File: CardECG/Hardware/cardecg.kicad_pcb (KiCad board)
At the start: 2 copper layers, 58 parts, among them CN1 2TAP, P1 PROG, P2 BATTERY, Q1 NTR1P02T1, Q2 NTR1P02T1, Q3 NTR1P02T1, Q4 NTR1P02T1, Q5 NMOS_GSD, Q6 NMOS_GSD, Q7 NTR1P02T1, Q8 NTR1P02T1, U1 LMV341, U2 TPS717, U3 ADuC7061, U4 SSD1306, U5 creditcard, U6 DNP, U7 DNP

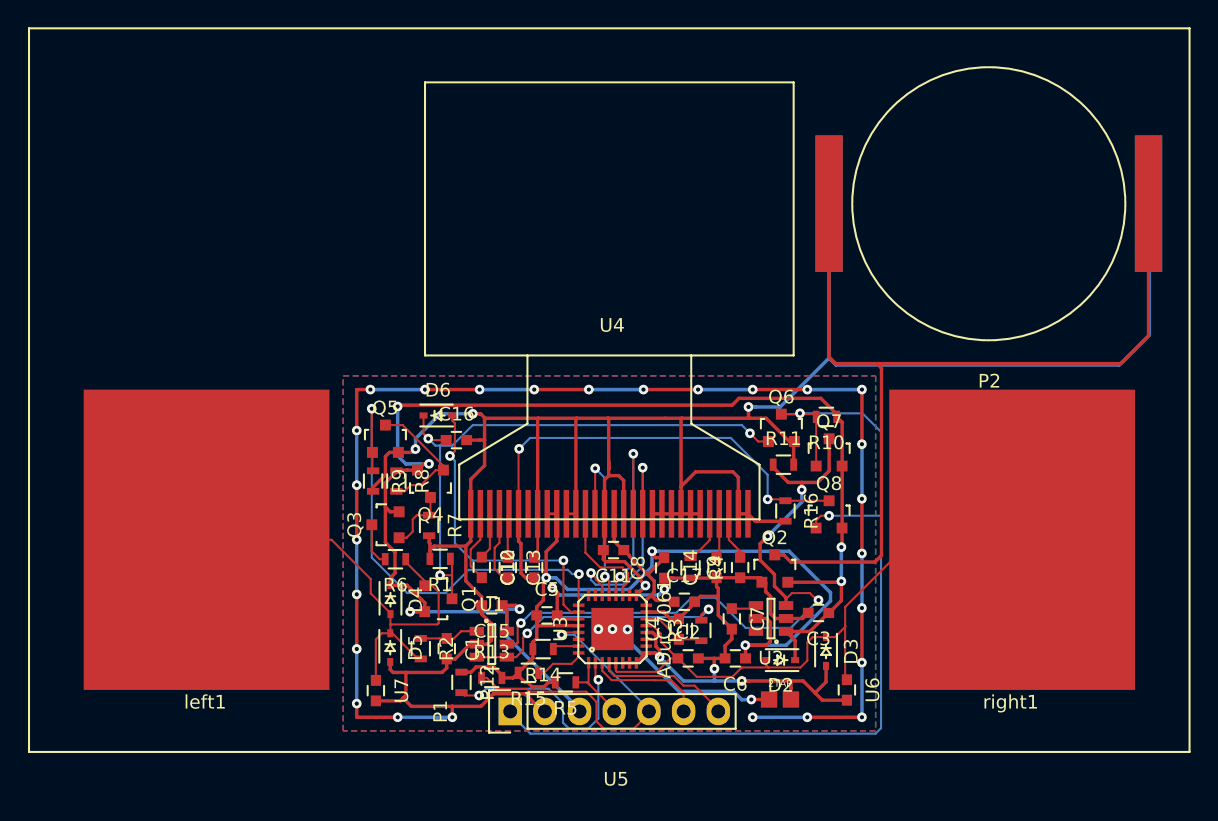
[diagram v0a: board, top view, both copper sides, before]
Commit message: Battery holder improvements.
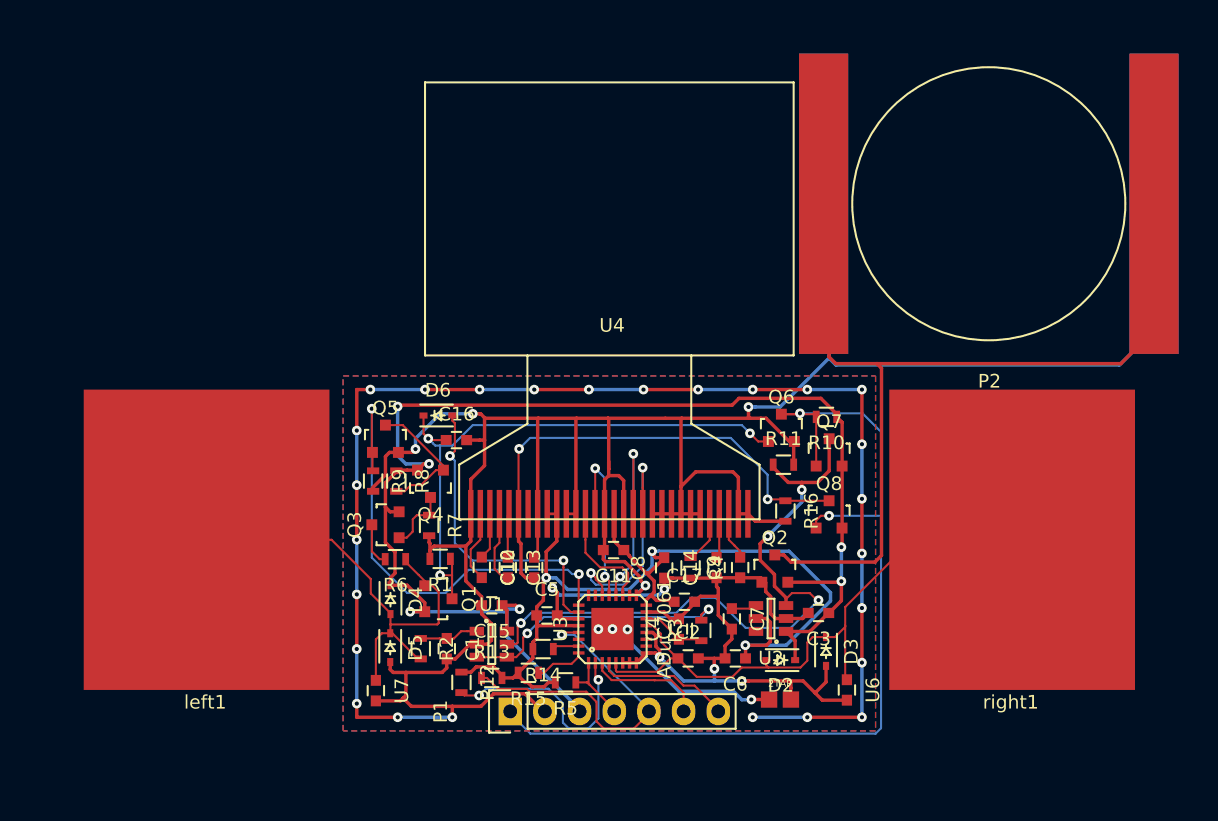
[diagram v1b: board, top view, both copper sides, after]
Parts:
- removed U5: creditcard, mod:creditcard
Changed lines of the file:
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@@
     (links 149)
     (no_connects 0)
-    (area 0 0 0 0)
+    (area 25.884199 22.770736 111.098001 77.062001)
     (thickness 1.6)
-    (drawings 12)
+    (drawings 14)
     (tracks 791)
     (zones 0)
-    (modules 58)
+    (modules 57)
     (nets 39)
   )
@@
     (pad_to_mask_clearance 0)
     (aux_axis_origin 0 0)
-    (visible_elements FFFFEF1F)
+    (visible_elements FFFFFF1F)
     (pcbplotparams
       (layerselection 0x020c0_80000001)
@@
     )
   )
-  (module mod:CR2016 (layer F.Cu)
-    (at 96.296678 36.848136)
-    (fp_text reference P2 (at 0.05 13) (layer F.SilkS)
-      (effects (font (size 1 1) (thickness 0.15)))
-    )
-    (fp_text value BATTERY (at 0 -13) (layer F.Fab)
-      (effects (font (size 1 1) (thickness 0.15)))
-    )
-    (fp_circle (center 0 0) (end 10 0) (layer F.SilkS) (width 0.15))
-    (pad 1 smd rect (at 11.7 0) (size 2 10) (layers F.Cu F.Paste F.Mask)
-      (net 29 "Net-(P2-Pad1)"))
-    (pad 2 smd rect (at -11.7 0) (size 2 10) (layers F.Cu F.Paste F.Mask)
-      (net 29 "Net-(P2-Pad1)"))
-    (pad 3 smd rect (at -11.7 0) (size 2 10) (layers B.Cu B.Paste B.Mask)
-      (net 3 GND))
-    (pad 4 smd rect (at 11.7 0) (size 2 10) (layers B.Cu B.Paste B.Mask)
-      (net 3 GND))
-  )
   (module mod:2TAP (layer F.Cu)
     (at 81.005278 73.159336)
@@
     )
   )
-  (module mod:creditcard (layer F.Cu)
-    (at 68 29)
-    (fp_text reference U5 (at 1 50) (layer F.SilkS)
-      (effects (font (size 1 1) (thickness 0.15)))
-    )
-    (fp_text value creditcard (at 0 -7) (layer F.Fab)
-      (effects (font (size 1 1) (thickness 0.15)))
-    )
-    (fp_line (start 43 48) (end 43 -5) (layer F.SilkS) (width 0.15))
-    (fp_line (start -42 48) (end 43 48) (layer F.SilkS) (width 0.15))
-    (fp_line (start -42 -5) (end -42 48) (layer F.SilkS) (width 0.15))
-    (fp_line (start 43 -5) (end -42 -5) (layer F.SilkS) (width 0.15))
-  )
   (module Capacitors_SMD:C_0603 (layer F.Cu)
     (at 57.305278 54.159336)
@@
     )
   )
-  (gr_line (start 25.9842 76.962) (end 25.9842 23.9522) (layer Margin) (width 0.2))
-  (gr_line (start 110.998 77.0128) (end 25.9842 76.962) (layer Margin) (width 0.2))
-  (gr_line (start 110.998 23.9776) (end 110.998 77.0128) (layer Margin) (width 0.2))
-  (gr_line (start 29.083 23.9776) (end 110.998 23.9776) (layer Margin) (width 0.2))
-  (gr_line (start 26.0096 23.9776) (end 29.083 23.9776) (layer Margin) (width 0.2))
+  (module mod:CR2016 (layer F.Cu)
+    (at 96.296678 36.848136)
+    (fp_text reference P2 (at 0.05 13) (layer F.SilkS)
+      (effects (font (size 1 1) (thickness 0.15)))
+    )
+    (fp_text value BATTERY (at 0 -13) (layer F.Fab)
+      (effects (font (size 1 1) (thickness 0.15)))
+    )
+    (fp_circle (center 0 0) (end 10 0) (layer F.SilkS) (width 0.15))
+    (pad 1 smd rect (at 12.1 0) (size 3.6 22) (layers F.Cu F.Paste F.Mask)
+      (net 29 "Net-(P2-Pad1)"))
+    (pad 2 smd rect (at -12.1 0) (size 3.6 22) (layers F.Cu F.Paste F.Mask)
+      (net 29 "Net-(P2-Pad1)"))
+    (pad 3 smd rect (at -12.1 0) (size 3.6 22) (layers B.Cu B.Paste B.Mask)
+      (net 3 GND))
+    (pad 4 smd rect (at 12.1 0) (size 3.6 22) (layers B.Cu B.Paste B.Mask)
+      (net 3 GND))
+  )
+  (gr_line (start 86.2965 23.9776) (end 25.9842 23.9776) (layer Margin) (width 0.2))
+  (gr_line (start 110.998 23.9776) (end 106.3117 23.9776) (layer Margin) (width 0.2))
+  (gr_line (start 106.3117 36.8427) (end 106.3117 23.9776) (layer Margin) (width 0.2))
+  (gr_line (start 86.2965 36.7665) (end 86.2965 23.9776) (layer Margin) (width 0.2))
+  (gr_arc (start 96.3 36.85) (end 106.31 36.85) (angle 180.7448032) (layer Margin) (width 0.2))
+  (gr_line (start 25.9842 76.962) (end 25.9842 23.9776) (layer Margin) (width 0.2))
+  (gr_line (start 110.998 76.962) (end 25.9842 76.962) (layer Margin) (width 0.2))
+  (gr_line (start 110.998 23.9776) (end 110.998 76.962) (layer Margin) (width 0.2))
   (gr_line (start 82.047278 27.983536) (end 54.996278 27.983536) (layer Margin) (width 0.2))
   (gr_line (start 82.021878 47.947936) (end 82.047278 27.983536) (layer Margin) (width 0.2))
@@
   (gr_line (start 55.021678 47.897136) (end 55.021678 47.947936) (layer Margin) (width 0.2))
   (gr_line (start 55.021678 27.958136) (end 55.021678 47.897136) (layer Margin) (width 0.2))
-  (gr_circle (center 96.296678 36.873536) (end 105.008878 42.156736) (layer Margin) (width 0.2))
   (segment (start 73.499878 70.147536) (end 73.524878 70.147536) (width 0.1524) (layer F.Cu) (net 1))
   (segment (start 72.268489 68.916147) (end 73.499878 70.147536) (width 0.1524) (layer F.Cu) (net 1))

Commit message: CardECG PCB fixes.
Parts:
- U1: footprint TO_SOT_Packages_SMD:SOT-23-6 -> TO_SOT_Packages_SMD:SC-70-6_Handsoldering
- U2: value TPS717 -> TPS71725; footprint TO_SOT_Packages_SMD:SOT-23-6 -> TO_SOT_Packages_SMD:SC-70-6_Handsoldering
- moved P2 2.25 mm to (96.3, 34.6)
- moved U1 0.50 mm to (59.5, 69.4), turned to 270 degrees
- moved C7 0.18 mm to (77.3, 67.3)
- turned U2 to 90 degrees
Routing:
- net GND: track 369.0 -> 583.4 mm, vias 35 -> 91
- net +BATT: track 103.5 -> 111.4 mm
- net OLED_PWR: track 36.3 -> 31.7 mm
- net Net-(U3-Pad20): track 15.3 -> 11.2 mm
- net Net-(C16-Pad1): track 43.1 -> 45.2 mm
- net Net-(U3-Pad21): track 13.1 -> 11.2 mm
- net Net-(U3-Pad22): track 17.6 -> 16.0 mm
- net Net-(C1-Pad1): track 4.33 -> 3.50 mm
- net Net-(R3-Pad2): track 20.1 -> 20.7 mm

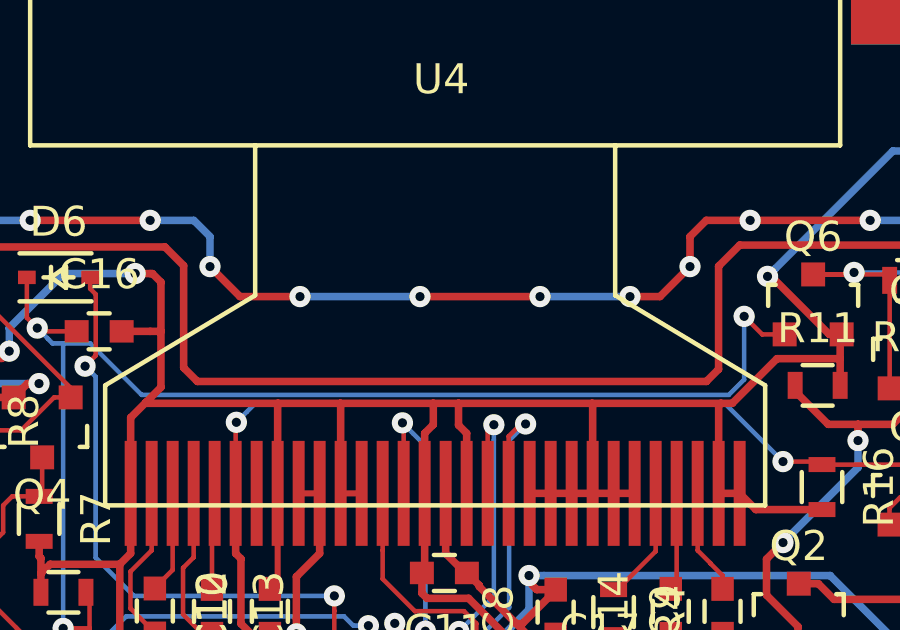
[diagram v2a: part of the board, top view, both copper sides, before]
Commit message: Bigger display cutout.
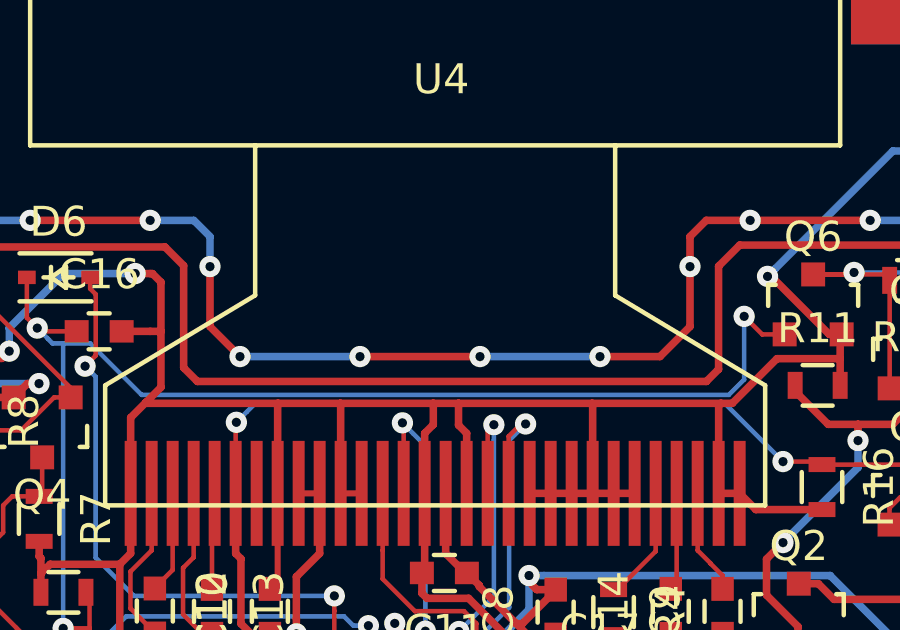
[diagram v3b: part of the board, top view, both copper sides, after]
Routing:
- net GND: track 583.4 -> 587.4 mm
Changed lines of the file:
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@@
     (thickness 1.6)
     (drawings 16)
-    (tracks 922)
+    (tracks 923)
     (zones 0)
     (modules 57)
@@
     )
   )
-  (gr_line (start 62 48.006) (end 62 51.5) (layer Margin) (width 0.2))
+  (gr_line (start 62 48.006) (end 62 53) (layer Margin) (width 0.2))
   (gr_line (start 61.976 48.006) (end 55.021678 48.006) (layer Margin) (width 0.2))
-  (gr_line (start 62 51.5) (end 75 51.5) (layer Margin) (width 0.2))
+  (gr_line (start 62 53) (end 75 53) (layer Margin) (width 0.2))
   (gr_line (start 55.021678 27.958136) (end 55.021678 48.006) (layer Margin) (width 0.2))
-  (gr_line (start 75 51.5) (end 75 48.006) (layer Margin) (width 0.2))
+  (gr_line (start 75 53) (end 75 48.006) (layer Margin) (width 0.2))
   (gr_line (start 82.047278 27.983536) (end 54.996278 27.983536) (layer Margin) (width 0.2))
   (gr_line (start 82.021878 48.006) (end 82.047278 27.983536) (layer Margin) (width 0.2))
@@
   (segment (start 56.596478 68.686336) (end 56.069078 68.686336) (width 0.1524) (layer F.Cu) (net 2))
   (segment (start 56.069078 68.686336) (end 54.691478 68.686336) (width 0.1524) (layer F.Cu) (net 2))
+  (segment (start 76 55) (end 77 54) (width 0.2524) (layer F.Cu) (net 3))
+  (segment (start 77 54) (end 77 52) (width 0.2524) (layer F.Cu) (net 3))
+  (segment (start 74 55) (end 76 55) (width 0.2524) (layer F.Cu) (net 3))
+  (segment (start 70 55) (end 74 55) (width 0.2524) (layer B.Cu) (net 3))
+  (via (at 74 55) (size 0.708) (drill 0.3048) (layers F.Cu B.Cu) (net 3))
+  (segment (start 66 55) (end 70 55) (width 0.2524) (layer F.Cu) (net 3))
+  (via (at 70 55) (size 0.708) (drill 0.3048) (layers F.Cu B.Cu) (net 3))
+  (segment (start 62 55) (end 66 55) (width 0.2524) (layer B.Cu) (net 3))
+  (via (at 66 55) (size 0.708) (drill 0.3048) (layers F.Cu B.Cu) (net 3))
+  (segment (start 61 52) (end 61 54) (width 0.2524) (layer F.Cu) (net 3))
+  (segment (start 61 54) (end 62 55) (width 0.2524) (layer F.Cu) (net 3))
+  (via (at 62 55) (size 0.708) (drill 0.3048) (layers F.Cu B.Cu) (net 3))
   (segment (start 56.596478 70.186336) (end 57.382814 69.4) (width 0.2524) (layer F.Cu) (net 3))
   (segment (start 57.382814 69.4) (end 58.16904 69.4) (width 0.2524) (layer F.Cu) (net 3))
@@
   (segment (start 53.005278 75.994722) (end 53 76) (width 0.2524) (layer F.Cu) (net 3))
   (via (at 53 76) (size 0.708) (drill 0.3048) (layers F.Cu B.Cu) (net 3))
-  (segment (start 75 53) (end 76 53) (width 0.2524) (layer F.Cu) (net 3))
-  (segment (start 76 53) (end 77 52) (width 0.2524) (layer F.Cu) (net 3))
-  (segment (start 72 53) (end 75 53) (width 0.2524) (layer B.Cu) (net 3))
-  (via (at 75 53) (size 0.708) (drill 0.3048) (layers F.Cu B.Cu) (net 3))
-  (segment (start 68 53) (end 72 53) (width 0.2524) (layer F.Cu) (net 3))
-  (via (at 72 53) (size 0.708) (drill 0.3048) (layers F.Cu B.Cu) (net 3))
-  (segment (start 64 53) (end 68 53) (width 0.2524) (layer B.Cu) (net 3))
-  (via (at 68 53) (size 0.708) (drill 0.3048) (layers F.Cu B.Cu) (net 3))
-  (segment (start 62 53) (end 64 53) (width 0.2524) (layer F.Cu) (net 3))
-  (via (at 64 53) (size 0.708) (drill 0.3048) (layers F.Cu B.Cu) (net 3))
-  (segment (start 61 52) (end 62 53) (width 0.2524) (layer F.Cu) (net 3))
   (segment (start 77.540664 50.459336) (end 77 51) (width 0.2524) (layer F.Cu) (net 3))
   (segment (start 77 51) (end 77 52) (width 0.2524) (layer F.Cu) (net 3))
@@
     (polygon
       (pts
-        (xy 54.5 27.5) (xy 82.5 27.5) (xy 82.5 48.5) (xy 75.5 48.5) (xy 75.5 52)
-        (xy 61.5 52) (xy 61.5 48.5) (xy 54.5 48.5)
+        (xy 54.5 27.5) (xy 82.5 27.5) (xy 82.5 48.5) (xy 75.5 48.5) (xy 75.5 53.5)
+        (xy 61.5 53.5) (xy 61.5 48.5) (xy 54.5 48.5)
       )
     )
@@
     (polygon
       (pts
-        (xy 54.5 27.5) (xy 82.5 27.5) (xy 82.5 48.5) (xy 75.5 48.5) (xy 75.5 52)
-        (xy 61.5 52) (xy 61.5 48.5) (xy 54.5 48.5)
+        (xy 54.5 27.5) (xy 82.5 27.5) (xy 82.5 48.5) (xy 75.5 48.5) (xy 75.5 53.5)
+        (xy 61.5 53.5) (xy 61.5 48.5) (xy 54.5 48.5)
       )
     )

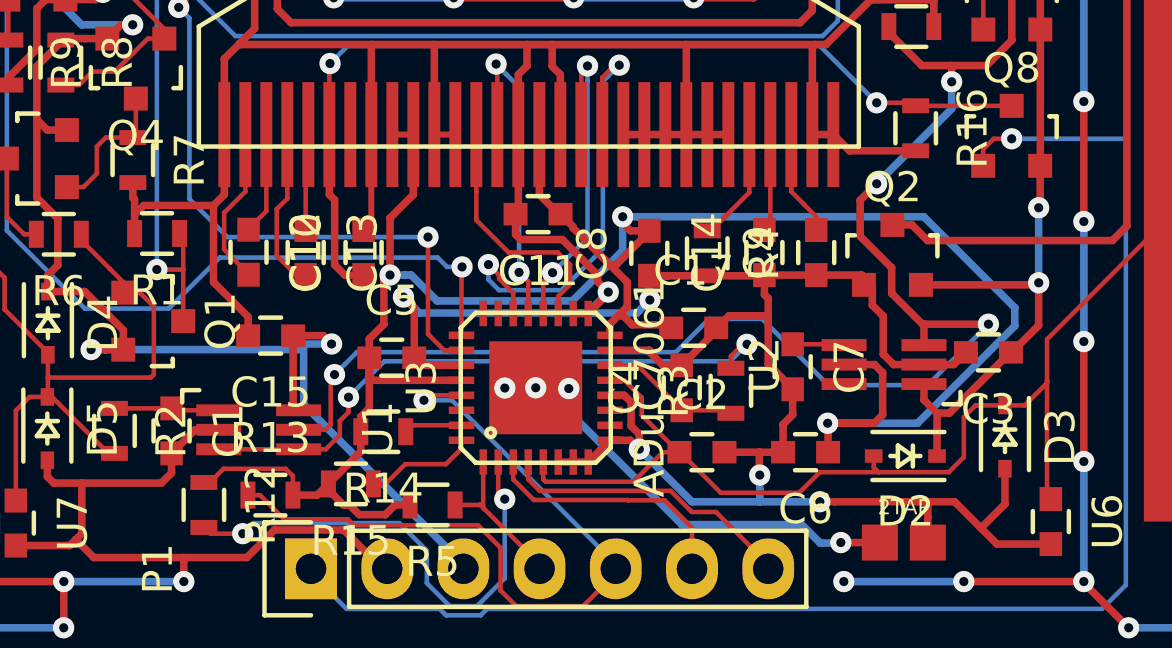
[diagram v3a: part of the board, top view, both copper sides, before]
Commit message: Fix LDO footprint. Modify makefile for FTDI UART.
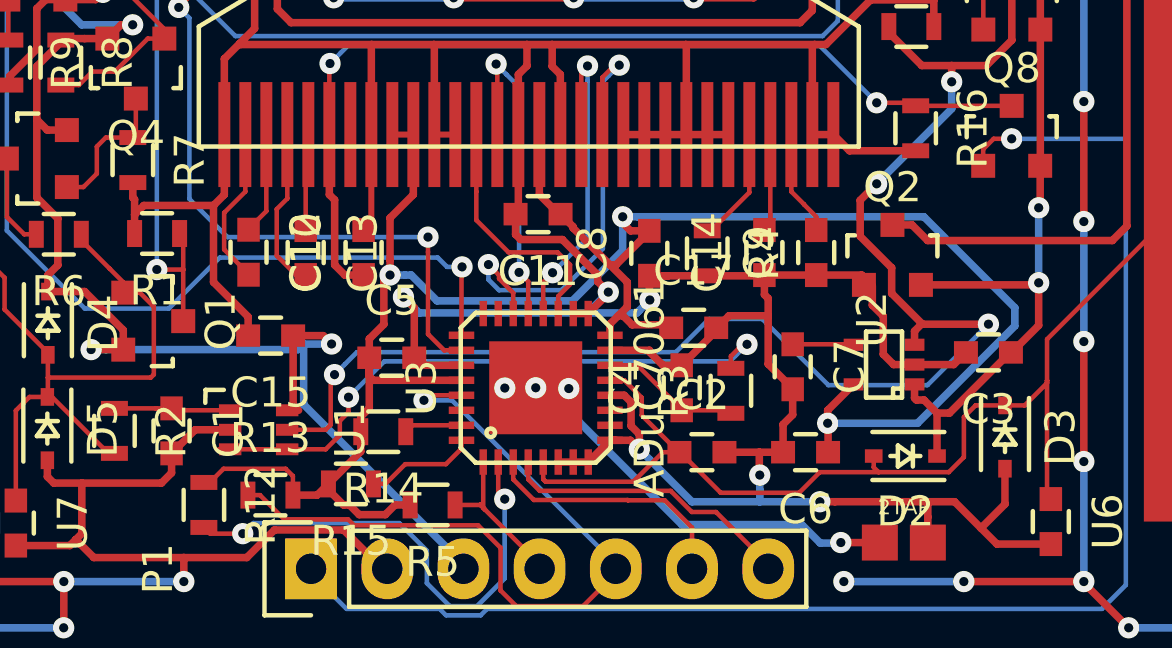
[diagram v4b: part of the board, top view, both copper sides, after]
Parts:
- Q1, Q3, Q4, Q7, Q8: value NTR1P02T1 -> TSM2311CX
- R3: value 4k -> 3.9k
- R5: value 47k -> 3.9k
- U1: footprint TO_SOT_Packages_SMD:SC-70-6_Handsoldering -> TO_SOT_Packages_SMD:SC-70-6
- U2: footprint TO_SOT_Packages_SMD:SC-70-6_Handsoldering -> TO_SOT_Packages_SMD:SC-70-5
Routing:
- net VDD: track 76.9 -> 74.0 mm
